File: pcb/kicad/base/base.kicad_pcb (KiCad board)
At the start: 2 copper layers, 348 parts, among them P1 J-Link SWD, P10 CONN_01X02, P11 CONN_01X02, P2 SMA, P3 CONN_01X02, P4 USB Micro B, P5 Button, P6 Button, P7 Button, P8 Button, P9 Button, Q1 IRLML2502, U1 SAMB11G18A-edit, U2 XBee-PRO_900HP, Y1 32.768kHz, Y2 26MHz

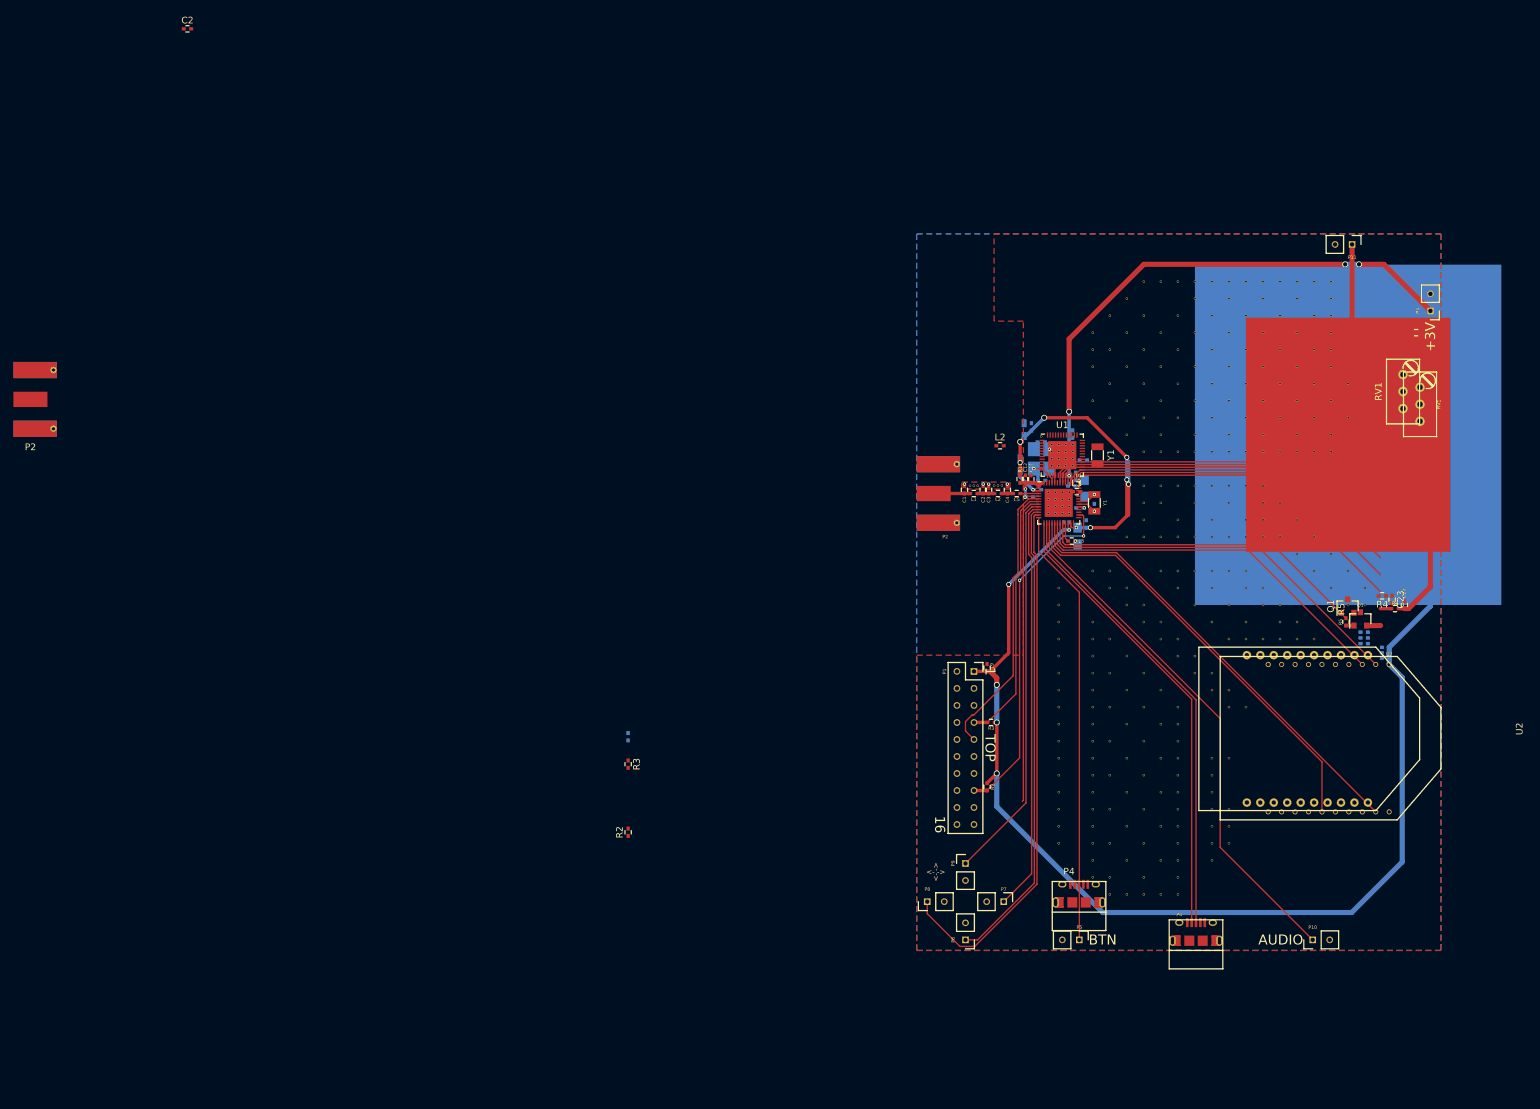
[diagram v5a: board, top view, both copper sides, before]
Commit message: Add stitch vias and fix silkscreen identifiers
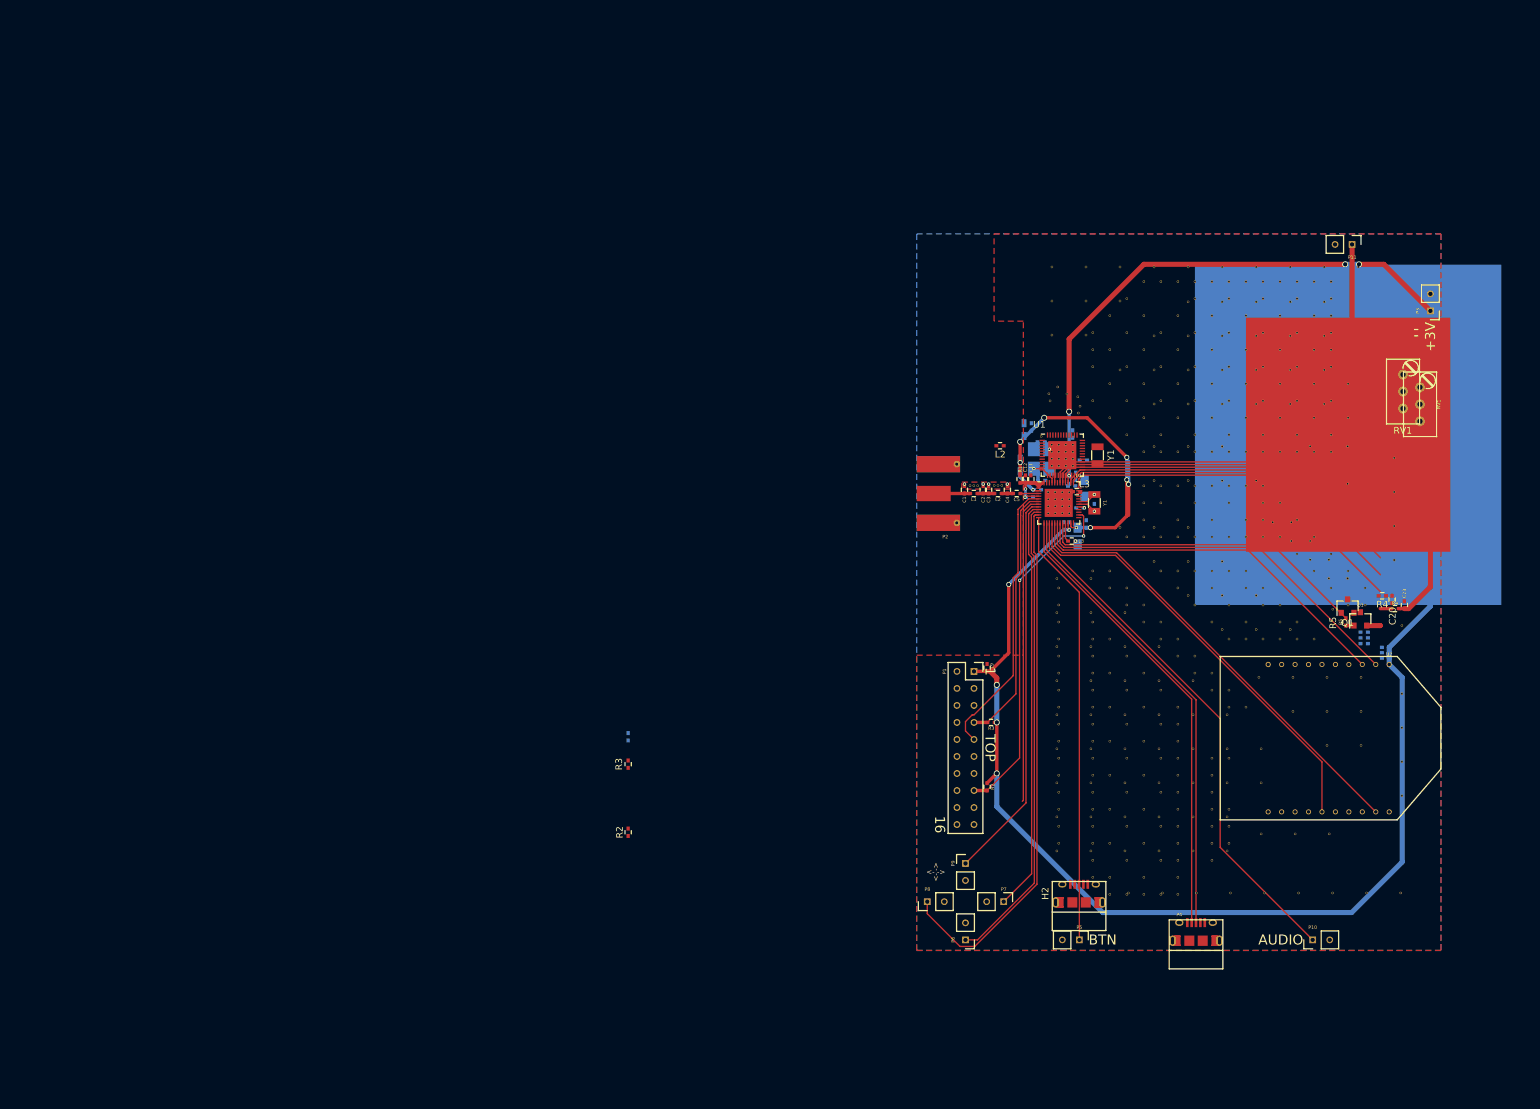
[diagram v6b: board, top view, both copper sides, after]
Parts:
- removed the C2 at (0.00, 0.00)
- removed the P2 at (-21.7, 55.3)
- removed the P4 at (133.1, 130.4)
- removed the U2 at (173.8, 104.5)
- added H2: USB Micro B, Connectors:USB_Micro-B_10118194-000XLF, F.Cu at (133.1, 130.4)
- added REF**: Via_Stitch_Dia0.356mm_Drill0.254mm, Misc:Via_Stitch_Dia0.356mm_Drill0.254mm, F.Cu at (181.1, 129.0)
- added REF**: Via_Stitch_Dia0.356mm_Drill0.254mm, Misc:Via_Stitch_Dia0.356mm_Drill0.254mm, F.Cu at (181.2, 114.5)
- added REF**: Via_Stitch_Dia0.356mm_Drill0.254mm, Misc:Via_Stitch_Dia0.356mm_Drill0.254mm, F.Cu at (144.2, 79.5)
- added REF**: Via_Stitch_Dia0.356mm_Drill0.254mm, Misc:Via_Stitch_Dia0.356mm_Drill0.254mm, F.Cu at (144.2, 74.4)
- added REF**: Via_Stitch_Dia0.356mm_Drill0.254mm, Misc:Via_Stitch_Dia0.356mm_Drill0.254mm, F.Cu at (149.3, 74.4)
- added REF**: Via_Stitch_Dia0.356mm_Drill0.254mm, Misc:Via_Stitch_Dia0.356mm_Drill0.254mm, F.Cu at (149.3, 79.5)
- added REF**: Via_Stitch_Dia0.356mm_Drill0.254mm, Misc:Via_Stitch_Dia0.356mm_Drill0.254mm, F.Cu at (169.6, 40.7)
- added REF**: Via_Stitch_Dia0.356mm_Drill0.254mm, Misc:Via_Stitch_Dia0.356mm_Drill0.254mm, F.Cu at (169.6, 45.8)
- added REF**: Via_Stitch_Dia0.356mm_Drill0.254mm, Misc:Via_Stitch_Dia0.356mm_Drill0.254mm, F.Cu at (169.6, 56.0)
- added REF**: Via_Stitch_Dia0.356mm_Drill0.254mm, Misc:Via_Stitch_Dia0.356mm_Drill0.254mm, F.Cu at (169.6, 50.9)
- added REF**: Via_Stitch_Dia0.356mm_Drill0.254mm, Misc:Via_Stitch_Dia0.356mm_Drill0.254mm, F.Cu at (164.6, 50.9)
- added REF**: Via_Stitch_Dia0.356mm_Drill0.254mm, Misc:Via_Stitch_Dia0.356mm_Drill0.254mm, F.Cu at (164.6, 56.0)
- added REF**: Via_Stitch_Dia0.356mm_Drill0.254mm, Misc:Via_Stitch_Dia0.356mm_Drill0.254mm, F.Cu at (181.2, 89.1)
- added REF**: Via_Stitch_Dia0.356mm_Drill0.254mm, Misc:Via_Stitch_Dia0.356mm_Drill0.254mm, F.Cu at (159.5, 56.0)
- added REF**: Via_Stitch_Dia0.356mm_Drill0.254mm, Misc:Via_Stitch_Dia0.356mm_Drill0.254mm, F.Cu at (159.5, 50.9)
- added REF**: Via_Stitch_Dia0.356mm_Drill0.254mm, Misc:Via_Stitch_Dia0.356mm_Drill0.254mm, F.Cu at (159.5, 40.7)
- added REF**: Via_Stitch_Dia0.356mm_Drill0.254mm, Misc:Via_Stitch_Dia0.356mm_Drill0.254mm, F.Cu at (159.5, 45.8)
- added REF**: Via_Stitch_Dia0.356mm_Drill0.254mm, Misc:Via_Stitch_Dia0.356mm_Drill0.254mm, F.Cu at (164.6, 45.8)
- added REF**: Via_Stitch_Dia0.356mm_Drill0.254mm, Misc:Via_Stitch_Dia0.356mm_Drill0.254mm, F.Cu at (164.6, 40.7)
- added REF**: Via_Stitch_Dia0.356mm_Drill0.254mm, Misc:Via_Stitch_Dia0.356mm_Drill0.254mm, F.Cu at (139.2, 50.9)
- added REF**: Via_Stitch_Dia0.356mm_Drill0.254mm, Misc:Via_Stitch_Dia0.356mm_Drill0.254mm, F.Cu at (154.4, 40.7)
- added REF**: Via_Stitch_Dia0.356mm_Drill0.254mm, Misc:Via_Stitch_Dia0.356mm_Drill0.254mm, F.Cu at (154.4, 45.8)
- added REF**: Via_Stitch_Dia0.356mm_Drill0.254mm, Misc:Via_Stitch_Dia0.356mm_Drill0.254mm, F.Cu at (149.3, 45.8)
- added REF**: Via_Stitch_Dia0.356mm_Drill0.254mm, Misc:Via_Stitch_Dia0.356mm_Drill0.254mm, F.Cu at (181.2, 109.4)
- added REF**: Via_Stitch_Dia0.356mm_Drill0.254mm, Misc:Via_Stitch_Dia0.356mm_Drill0.254mm, F.Cu at (149.3, 40.7)
- added REF**: Via_Stitch_Dia0.356mm_Drill0.254mm, Misc:Via_Stitch_Dia0.356mm_Drill0.254mm, F.Cu at (144.2, 45.8)
- added REF**: Via_Stitch_Dia0.356mm_Drill0.254mm, Misc:Via_Stitch_Dia0.356mm_Drill0.254mm, F.Cu at (144.2, 56.0)
- added REF**: Via_Stitch_Dia0.356mm_Drill0.254mm, Misc:Via_Stitch_Dia0.356mm_Drill0.254mm, F.Cu at (144.2, 50.9)
- added REF**: Via_Stitch_Dia0.356mm_Drill0.254mm, Misc:Via_Stitch_Dia0.356mm_Drill0.254mm, F.Cu at (149.3, 50.9)
- added REF**: Via_Stitch_Dia0.356mm_Drill0.254mm, Misc:Via_Stitch_Dia0.356mm_Drill0.254mm, F.Cu at (149.3, 56.0)
- added REF**: Via_Stitch_Dia0.356mm_Drill0.254mm, Misc:Via_Stitch_Dia0.356mm_Drill0.254mm, F.Cu at (154.4, 56.0)
- added REF**: Via_Stitch_Dia0.356mm_Drill0.254mm, Misc:Via_Stitch_Dia0.356mm_Drill0.254mm, F.Cu at (154.4, 50.9)
- added REF**: Via_Stitch_Dia0.356mm_Drill0.254mm, Misc:Via_Stitch_Dia0.356mm_Drill0.254mm, F.Cu at (159.5, 67.4)
- added REF**: Via_Stitch_Dia0.356mm_Drill0.254mm, Misc:Via_Stitch_Dia0.356mm_Drill0.254mm, F.Cu at (154.4, 62.3)
- added REF**: Via_Stitch_Dia0.356mm_Drill0.254mm, Misc:Via_Stitch_Dia0.356mm_Drill0.254mm, F.Cu at (181.2, 104.3)
- added REF**: Via_Stitch_Dia0.356mm_Drill0.254mm, Misc:Via_Stitch_Dia0.356mm_Drill0.254mm, F.Cu at (154.4, 67.4)
- added REF**: Via_Stitch_Dia0.356mm_Drill0.254mm, Misc:Via_Stitch_Dia0.356mm_Drill0.254mm, F.Cu at (149.3, 67.4)
- added REF**: Via_Stitch_Dia0.356mm_Drill0.254mm, Misc:Via_Stitch_Dia0.356mm_Drill0.254mm, F.Cu at (149.3, 62.3)
- added REF**: Via_Stitch_Dia0.356mm_Drill0.254mm, Misc:Via_Stitch_Dia0.356mm_Drill0.254mm, F.Cu at (144.2, 62.3)
- added REF**: Via_Stitch_Dia0.356mm_Drill0.254mm, Misc:Via_Stitch_Dia0.356mm_Drill0.254mm, F.Cu at (144.2, 67.4)
- added REF**: Via_Stitch_Dia0.356mm_Drill0.254mm, Misc:Via_Stitch_Dia0.356mm_Drill0.254mm, F.Cu at (173.1, 62.3)
- added REF**: Via_Stitch_Dia0.356mm_Drill0.254mm, Misc:Via_Stitch_Dia0.356mm_Drill0.254mm, F.Cu at (173.1, 67.9)
- added REF**: Via_Stitch_Dia0.356mm_Drill0.254mm, Misc:Via_Stitch_Dia0.356mm_Drill0.254mm, F.Cu at (167.5, 62.3)
- added REF**: Via_Stitch_Dia0.356mm_Drill0.254mm, Misc:Via_Stitch_Dia0.356mm_Drill0.254mm, F.Cu at (167.5, 76.4)
- added REF**: Via_Stitch_Dia0.356mm_Drill0.254mm, Misc:Via_Stitch_Dia0.356mm_Drill0.254mm, F.Cu at (164.7, 76.4)
- added REF**: Via_Stitch_Dia0.356mm_Drill0.254mm, Misc:Via_Stitch_Dia0.356mm_Drill0.254mm, F.Cu at (181.2, 99.2)
- added REF**: Via_Stitch_Dia0.356mm_Drill0.254mm, Misc:Via_Stitch_Dia0.356mm_Drill0.254mm, F.Cu at (162.0, 73.6)
- added REF**: Via_Stitch_Dia0.356mm_Drill0.254mm, Misc:Via_Stitch_Dia0.356mm_Drill0.254mm, F.Cu at (164.7, 73.6)
- added REF**: Via_Stitch_Dia0.356mm_Drill0.254mm, Misc:Via_Stitch_Dia0.356mm_Drill0.254mm, F.Cu at (170.3, 79.2)
- added REF**: Via_Stitch_Dia0.356mm_Drill0.254mm, Misc:Via_Stitch_Dia0.356mm_Drill0.254mm, F.Cu at (167.5, 79.2)
- added REF**: Via_Stitch_Dia0.356mm_Drill0.254mm, Misc:Via_Stitch_Dia0.356mm_Drill0.254mm, F.Cu at (170.3, 82.0)
- added REF**: Via_Stitch_Dia0.356mm_Drill0.254mm, Misc:Via_Stitch_Dia0.356mm_Drill0.254mm, F.Cu at (173.1, 82.0)
- added REF**: Via_Stitch_Dia0.356mm_Drill0.254mm, Misc:Via_Stitch_Dia0.356mm_Drill0.254mm, F.Cu at (132.9, 54.9)
- added REF**: Via_Stitch_Dia0.356mm_Drill0.254mm, Misc:Via_Stitch_Dia0.356mm_Drill0.254mm, F.Cu at (129.9, 53.4)
- added REF**: Via_Stitch_Dia0.356mm_Drill0.254mm, Misc:Via_Stitch_Dia0.356mm_Drill0.254mm, F.Cu at (128.5, 54.5)
- added REF**: Via_Stitch_Dia0.356mm_Drill0.254mm, Misc:Via_Stitch_Dia0.356mm_Drill0.254mm, F.Cu at (131.2, 54.5)
- added REF**: Via_Stitch_Dia0.356mm_Drill0.254mm, Misc:Via_Stitch_Dia0.356mm_Drill0.254mm, F.Cu at (129.7, 122.7)
- added REF**: Via_Stitch_Dia0.356mm_Drill0.254mm, Misc:Via_Stitch_Dia0.356mm_Drill0.254mm, F.Cu at (133.2, 56.3)
- added REF**: Via_Stitch_Dia0.356mm_Drill0.254mm, Misc:Via_Stitch_Dia0.356mm_Drill0.254mm, F.Cu at (132.9, 57.3)
- added REF**: Via_Stitch_Dia0.356mm_Drill0.254mm, Misc:Via_Stitch_Dia0.356mm_Drill0.254mm, F.Cu at (129.7, 117.6)
- added REF**: Via_Stitch_Dia0.356mm_Drill0.254mm, Misc:Via_Stitch_Dia0.356mm_Drill0.254mm, F.Cu at (129.7, 107.4)
- added REF**: Via_Stitch_Dia0.356mm_Drill0.254mm, Misc:Via_Stitch_Dia0.356mm_Drill0.254mm, F.Cu at (129.7, 112.5)
- added REF**: Via_Stitch_Dia0.356mm_Drill0.254mm, Misc:Via_Stitch_Dia0.356mm_Drill0.254mm, F.Cu at (129.7, 97.3)
- added REF**: Via_Stitch_Dia0.356mm_Drill0.254mm, Misc:Via_Stitch_Dia0.356mm_Drill0.254mm, F.Cu at (160.7, 129.0)
- added REF**: Via_Stitch_Dia0.356mm_Drill0.254mm, Misc:Via_Stitch_Dia0.356mm_Drill0.254mm, F.Cu at (129.7, 92.2)
- added REF**: Via_Stitch_Dia0.356mm_Drill0.254mm, Misc:Via_Stitch_Dia0.356mm_Drill0.254mm, F.Cu at (129.7, 102.4)
- added REF**: Via_Stitch_Dia0.356mm_Drill0.254mm, Misc:Via_Stitch_Dia0.356mm_Drill0.254mm, F.Cu at (129.7, 87.1)
- added REF**: Via_Stitch_Dia0.356mm_Drill0.254mm, Misc:Via_Stitch_Dia0.356mm_Drill0.254mm, F.Cu at (129.7, 82.0)
- added REF**: Via_Stitch_Dia0.356mm_Drill0.254mm, Misc:Via_Stitch_Dia0.356mm_Drill0.254mm, F.Cu at (180.1, 79.3)
- added REF**: Via_Stitch_Dia0.356mm_Drill0.254mm, Misc:Via_Stitch_Dia0.356mm_Drill0.254mm, F.Cu at (180.1, 74.2)
- added REF**: Via_Stitch_Dia0.356mm_Drill0.254mm, Misc:Via_Stitch_Dia0.356mm_Drill0.254mm, F.Cu at (180.1, 64.0)
- added REF**: Via_Stitch_Dia0.356mm_Drill0.254mm, Misc:Via_Stitch_Dia0.356mm_Drill0.254mm, F.Cu at (180.1, 69.1)
- added REF**: Via_Stitch_Dia0.356mm_Drill0.254mm, Misc:Via_Stitch_Dia0.356mm_Drill0.254mm, F.Cu at (129.0, 45.7)
- added REF**: Via_Stitch_Dia0.356mm_Drill0.254mm, Misc:Via_Stitch_Dia0.356mm_Drill0.254mm, F.Cu at (134.1, 45.7)
- added REF**: Via_Stitch_Dia0.356mm_Drill0.254mm, Misc:Via_Stitch_Dia0.356mm_Drill0.254mm, F.Cu at (165.8, 129.0)
- added REF**: Via_Stitch_Dia0.356mm_Drill0.254mm, Misc:Via_Stitch_Dia0.356mm_Drill0.254mm, F.Cu at (129.0, 35.5)
- added REF**: Via_Stitch_Dia0.356mm_Drill0.254mm, Misc:Via_Stitch_Dia0.356mm_Drill0.254mm, F.Cu at (134.1, 35.5)
- added REF**: Via_Stitch_Dia0.356mm_Drill0.254mm, Misc:Via_Stitch_Dia0.356mm_Drill0.254mm, F.Cu at (134.1, 40.6)
- added REF**: Via_Stitch_Dia0.356mm_Drill0.254mm, Misc:Via_Stitch_Dia0.356mm_Drill0.254mm, F.Cu at (129.0, 40.6)
- added REF**: Via_Stitch_Dia0.356mm_Drill0.254mm, Misc:Via_Stitch_Dia0.356mm_Drill0.254mm, F.Cu at (139.2, 40.6)
- added REF**: Via_Stitch_Dia0.356mm_Drill0.254mm, Misc:Via_Stitch_Dia0.356mm_Drill0.254mm, F.Cu at (154.4, 35.5)
- added REF**: Via_Stitch_Dia0.356mm_Drill0.254mm, Misc:Via_Stitch_Dia0.356mm_Drill0.254mm, F.Cu at (149.3, 35.5)
- added REF**: Via_Stitch_Dia0.356mm_Drill0.254mm, Misc:Via_Stitch_Dia0.356mm_Drill0.254mm, F.Cu at (139.2, 35.5)
- added REF**: Via_Stitch_Dia0.356mm_Drill0.254mm, Misc:Via_Stitch_Dia0.356mm_Drill0.254mm, F.Cu at (144.2, 35.5)
- added REF**: Via_Stitch_Dia0.356mm_Drill0.254mm, Misc:Via_Stitch_Dia0.356mm_Drill0.254mm, F.Cu at (164.6, 35.5)
- added REF**: Via_Stitch_Dia0.356mm_Drill0.254mm, Misc:Via_Stitch_Dia0.356mm_Drill0.254mm, F.Cu at (176.0, 129.0)
- added REF**: Via_Stitch_Dia0.356mm_Drill0.254mm, Misc:Via_Stitch_Dia0.356mm_Drill0.254mm, F.Cu at (159.5, 35.5)
- added REF**: Via_Stitch_Dia0.356mm_Drill0.254mm, Misc:Via_Stitch_Dia0.356mm_Drill0.254mm, F.Cu at (169.6, 35.5)
- added REF**: Via_Stitch_Dia0.356mm_Drill0.254mm, Misc:Via_Stitch_Dia0.356mm_Drill0.254mm, F.Cu at (174.7, 35.5)
- added REF**: Via_Stitch_Dia0.356mm_Drill0.254mm, Misc:Via_Stitch_Dia0.356mm_Drill0.254mm, F.Cu at (128.7, 55.5)
- added REF**: Via_Stitch_Dia0.356mm_Drill0.254mm, Misc:Via_Stitch_Dia0.356mm_Drill0.254mm, F.Cu at (170.1, 106.9)
- added REF**: Via_Stitch_Dia0.356mm_Drill0.254mm, Misc:Via_Stitch_Dia0.356mm_Drill0.254mm, F.Cu at (175.1, 106.9)
- added REF**: Via_Stitch_Dia0.356mm_Drill0.254mm, Misc:Via_Stitch_Dia0.356mm_Drill0.254mm, F.Cu at (175.1, 101.9)
- added REF**: Via_Stitch_Dia0.356mm_Drill0.254mm, Misc:Via_Stitch_Dia0.356mm_Drill0.254mm, F.Cu at (165.0, 101.9)
- added REF**: Via_Stitch_Dia0.356mm_Drill0.254mm, Misc:Via_Stitch_Dia0.356mm_Drill0.254mm, F.Cu at (170.1, 101.9)
- added REF**: Via_Stitch_Dia0.356mm_Drill0.254mm, Misc:Via_Stitch_Dia0.356mm_Drill0.254mm, F.Cu at (165.0, 96.8)
- added REF**: Via_Stitch_Dia0.356mm_Drill0.254mm, Misc:Via_Stitch_Dia0.356mm_Drill0.254mm, F.Cu at (159.9, 96.8)
- added REF**: Via_Stitch_Dia0.356mm_Drill0.254mm, Misc:Via_Stitch_Dia0.356mm_Drill0.254mm, F.Cu at (170.9, 129.0)
- added REF**: Via_Stitch_Dia0.356mm_Drill0.254mm, Misc:Via_Stitch_Dia0.356mm_Drill0.254mm, F.Cu at (170.1, 96.8)
- added REF**: Via_Stitch_Dia0.356mm_Drill0.254mm, Misc:Via_Stitch_Dia0.356mm_Drill0.254mm, F.Cu at (175.1, 96.8)
- added REF**: Via_Stitch_Dia0.356mm_Drill0.254mm, Misc:Via_Stitch_Dia0.356mm_Drill0.254mm, F.Cu at (170.4, 120.1)
- added REF**: Via_Stitch_Dia0.356mm_Drill0.254mm, Misc:Via_Stitch_Dia0.356mm_Drill0.254mm, F.Cu at (155.1, 117.6)
- added REF**: Via_Stitch_Dia0.356mm_Drill0.254mm, Misc:Via_Stitch_Dia0.356mm_Drill0.254mm, F.Cu at (155.1, 122.7)
- added REF**: Via_Stitch_Dia0.356mm_Drill0.254mm, Misc:Via_Stitch_Dia0.356mm_Drill0.254mm, F.Cu at (165.3, 120.1)
- added REF**: Via_Stitch_Dia0.356mm_Drill0.254mm, Misc:Via_Stitch_Dia0.356mm_Drill0.254mm, F.Cu at (160.2, 120.1)
- added REF**: Via_Stitch_Dia0.356mm_Drill0.254mm, Misc:Via_Stitch_Dia0.356mm_Drill0.254mm, F.Cu at (160.2, 112.5)
- added REF**: Via_Stitch_Dia0.356mm_Drill0.254mm, Misc:Via_Stitch_Dia0.356mm_Drill0.254mm, F.Cu at (160.2, 107.4)
- added REF**: Via_Stitch_Dia0.356mm_Drill0.254mm, Misc:Via_Stitch_Dia0.356mm_Drill0.254mm, F.Cu at (155.1, 107.4)
- added REF**: Via_Stitch_Dia0.356mm_Drill0.254mm, Misc:Via_Stitch_Dia0.356mm_Drill0.254mm, F.Cu at (150.6, 129.0)
- added REF**: Via_Stitch_Dia0.356mm_Drill0.254mm, Misc:Via_Stitch_Dia0.356mm_Drill0.254mm, F.Cu at (155.1, 112.5)
- added REF**: Via_Stitch_Dia0.356mm_Drill0.254mm, Misc:Via_Stitch_Dia0.356mm_Drill0.254mm, F.Cu at (155.1, 102.4)
- added REF**: Via_Stitch_Dia0.356mm_Drill0.254mm, Misc:Via_Stitch_Dia0.356mm_Drill0.254mm, F.Cu at (134.8, 82.0)
- added REF**: Via_Stitch_Dia0.356mm_Drill0.254mm, Misc:Via_Stitch_Dia0.356mm_Drill0.254mm, F.Cu at (134.8, 87.1)
- added REF**: Via_Stitch_Dia0.356mm_Drill0.254mm, Misc:Via_Stitch_Dia0.356mm_Drill0.254mm, F.Cu at (139.9, 87.1)
- added REF**: Via_Stitch_Dia0.356mm_Drill0.254mm, Misc:Via_Stitch_Dia0.356mm_Drill0.254mm, F.Cu at (134.8, 102.4)
- added REF**: Via_Stitch_Dia0.356mm_Drill0.254mm, Misc:Via_Stitch_Dia0.356mm_Drill0.254mm, F.Cu at (139.9, 102.4)
- added REF**: Via_Stitch_Dia0.356mm_Drill0.254mm, Misc:Via_Stitch_Dia0.356mm_Drill0.254mm, F.Cu at (139.9, 97.3)
- added REF**: Via_Stitch_Dia0.356mm_Drill0.254mm, Misc:Via_Stitch_Dia0.356mm_Drill0.254mm, F.Cu at (139.9, 92.2)
- added REF**: Via_Stitch_Dia0.356mm_Drill0.254mm, Misc:Via_Stitch_Dia0.356mm_Drill0.254mm, F.Cu at (134.8, 92.2)
- added REF**: Via_Stitch_Dia0.356mm_Drill0.254mm, Misc:Via_Stitch_Dia0.356mm_Drill0.254mm, F.Cu at (155.7, 129.0)
- added REF**: Via_Stitch_Dia0.356mm_Drill0.254mm, Misc:Via_Stitch_Dia0.356mm_Drill0.254mm, F.Cu at (134.8, 97.3)
- added REF**: Via_Stitch_Dia0.356mm_Drill0.254mm, Misc:Via_Stitch_Dia0.356mm_Drill0.254mm, F.Cu at (145.0, 97.3)
- added REF**: Via_Stitch_Dia0.356mm_Drill0.254mm, Misc:Via_Stitch_Dia0.356mm_Drill0.254mm, F.Cu at (145.0, 92.2)
- added REF**: Via_Stitch_Dia0.356mm_Drill0.254mm, Misc:Via_Stitch_Dia0.356mm_Drill0.254mm, F.Cu at (150.1, 97.3)
- added REF**: Via_Stitch_Dia0.356mm_Drill0.254mm, Misc:Via_Stitch_Dia0.356mm_Drill0.254mm, F.Cu at (150.1, 102.4)
- added REF**: Via_Stitch_Dia0.356mm_Drill0.254mm, Misc:Via_Stitch_Dia0.356mm_Drill0.254mm, F.Cu at (145.0, 102.4)
- added REF**: Via_Stitch_Dia0.356mm_Drill0.254mm, Misc:Via_Stitch_Dia0.356mm_Drill0.254mm, F.Cu at (145.0, 122.7)
- added REF**: Via_Stitch_Dia0.356mm_Drill0.254mm, Misc:Via_Stitch_Dia0.356mm_Drill0.254mm, F.Cu at (145.0, 117.6)
- added REF**: Via_Stitch_Dia0.356mm_Drill0.254mm, Misc:Via_Stitch_Dia0.356mm_Drill0.254mm, F.Cu at (150.1, 117.6)
- added REF**: Via_Stitch_Dia0.356mm_Drill0.254mm, Misc:Via_Stitch_Dia0.356mm_Drill0.254mm, F.Cu at (150.1, 122.7)
- added REF**: Via_Stitch_Dia0.356mm_Drill0.254mm, Misc:Via_Stitch_Dia0.356mm_Drill0.254mm, F.Cu at (145.5, 129.0)
- added REF**: Via_Stitch_Dia0.356mm_Drill0.254mm, Misc:Via_Stitch_Dia0.356mm_Drill0.254mm, F.Cu at (150.1, 112.5)
- added REF**: Via_Stitch_Dia0.356mm_Drill0.254mm, Misc:Via_Stitch_Dia0.356mm_Drill0.254mm, F.Cu at (150.1, 107.4)
- added REF**: Via_Stitch_Dia0.356mm_Drill0.254mm, Misc:Via_Stitch_Dia0.356mm_Drill0.254mm, F.Cu at (145.0, 107.4)
- added REF**: Via_Stitch_Dia0.356mm_Drill0.254mm, Misc:Via_Stitch_Dia0.356mm_Drill0.254mm, F.Cu at (145.0, 112.5)
- added REF**: Via_Stitch_Dia0.356mm_Drill0.254mm, Misc:Via_Stitch_Dia0.356mm_Drill0.254mm, F.Cu at (134.8, 112.5)
- added REF**: Via_Stitch_Dia0.356mm_Drill0.254mm, Misc:Via_Stitch_Dia0.356mm_Drill0.254mm, F.Cu at (134.8, 107.4)
- added REF**: Via_Stitch_Dia0.356mm_Drill0.254mm, Misc:Via_Stitch_Dia0.356mm_Drill0.254mm, F.Cu at (139.9, 107.4)
- added REF**: Via_Stitch_Dia0.356mm_Drill0.254mm, Misc:Via_Stitch_Dia0.356mm_Drill0.254mm, F.Cu at (139.9, 112.5)
- added REF**: Via_Stitch_Dia0.356mm_Drill0.254mm, Misc:Via_Stitch_Dia0.356mm_Drill0.254mm, F.Cu at (139.9, 122.7)
- added REF**: Via_Stitch_Dia0.356mm_Drill0.254mm, Misc:Via_Stitch_Dia0.356mm_Drill0.254mm, F.Cu at (139.9, 117.6)
- added REF**: Via_Stitch_Dia0.356mm_Drill0.254mm, Misc:Via_Stitch_Dia0.356mm_Drill0.254mm, F.Cu at (140.4, 129.0)
- added REF**: Via_Stitch_Dia0.356mm_Drill0.254mm, Misc:Via_Stitch_Dia0.356mm_Drill0.254mm, F.Cu at (134.8, 117.6)
- added REF**: Via_Stitch_Dia0.356mm_Drill0.254mm, Misc:Via_Stitch_Dia0.356mm_Drill0.254mm, F.Cu at (134.8, 122.7)
- added REF**: Via_Stitch_Dia0.356mm_Drill0.254mm, Misc:Via_Stitch_Dia0.356mm_Drill0.254mm, F.Cu at (164.6, 89.6)
- added REF**: Via_Stitch_Dia0.356mm_Drill0.254mm, Misc:Via_Stitch_Dia0.356mm_Drill0.254mm, F.Cu at (154.4, 79.5)
- added REF**: Via_Stitch_Dia0.356mm_Drill0.254mm, Misc:Via_Stitch_Dia0.356mm_Drill0.254mm, F.Cu at (149.3, 84.6)
- added REF**: Via_Stitch_Dia0.356mm_Drill0.254mm, Misc:Via_Stitch_Dia0.356mm_Drill0.254mm, F.Cu at (159.5, 89.6)
- added REF**: Via_Stitch_Dia0.356mm_Drill0.254mm, Misc:Via_Stitch_Dia0.356mm_Drill0.254mm, F.Cu at (159.5, 84.6)
- added REF**: Via_Stitch_Dia0.356mm_Drill0.254mm, Misc:Via_Stitch_Dia0.356mm_Drill0.254mm, F.Cu at (154.4, 84.6)
- added REF**: Via_Stitch_Dia0.356mm_Drill0.254mm, Misc:Via_Stitch_Dia0.356mm_Drill0.254mm, F.Cu at (154.4, 89.6)
- added REF**: Via_Stitch_Dia0.356mm_Drill0.254mm, Misc:Via_Stitch_Dia0.356mm_Drill0.254mm, F.Cu at (139.2, 74.4)
- C19: value C_Small -> 1.0uF
- C20: value 47pF -> 1.0uF; moved to F.Cu
- C21: value 1.0uF -> 47pF
- C22: value 10uF -> 1.0uF
- C23: value 1.0uF -> 10uF; moved to B.Cu
- moved C20 7.78 mm to (179.8, 85.2), turned to 270 degrees
- moved C23 6.41 mm to (175.6, 90.0), turned to 180 degrees
- moved C21 0.85 mm to (175.6, 91.7)
- moved C22 0.85 mm to (175.6, 90.9)
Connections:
- C20 pad 1: /+3.3V -> /+5V
- C23 pad 1: /+5V -> /+3.3V
- L2 pad 1: Net-(C2-Pad1) -> /SIG_2.4G
- REF** pad 1: (no net) -> /SIG_2.4G
- U1 pad 42: (no net) -> GND
- U1 pad 43: (no net) -> GND
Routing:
- net /SWDIO: track 0.00 -> 291.8 mm, vias 0 -> 9
- net /+3.3V: track 291.8 -> 0.99 mm, vias 9 -> 1
- net Net-(L3-Pad1): track 65.5 -> 0.00 mm
- net Net-(L3-Pad2): track 2.86 -> 65.5 mm
- net Net-(C18-Pad1): track 0.99 -> 43.9 mm, vias 1 -> 7
- net /+5V: track 0.00 -> 42.0 mm
- net Net-(C14-Pad1): track 43.9 -> 4.55 mm, vias 7 -> 1
- net /SWDCLK: track 38.9 -> 0.00 mm
- net Net-(C13-Pad1): track 4.55 -> 10.3 mm, vias 1 -> 2
- net Net-(C8-Pad1): track 7.20 -> 2.75 mm
- net Net-(C10-Pad1): track 10.3 -> 5.95 mm, vias 2 -> 1
- net /SWO: track 42.0 -> 38.9 mm
- net /UART_RTS: track 0.00 -> 2.86 mm
- net Net-(C2-Pad1): track 2.51 -> 0.00 mm
- net Net-(C9-Pad1): track 5.95 -> 7.20 mm
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
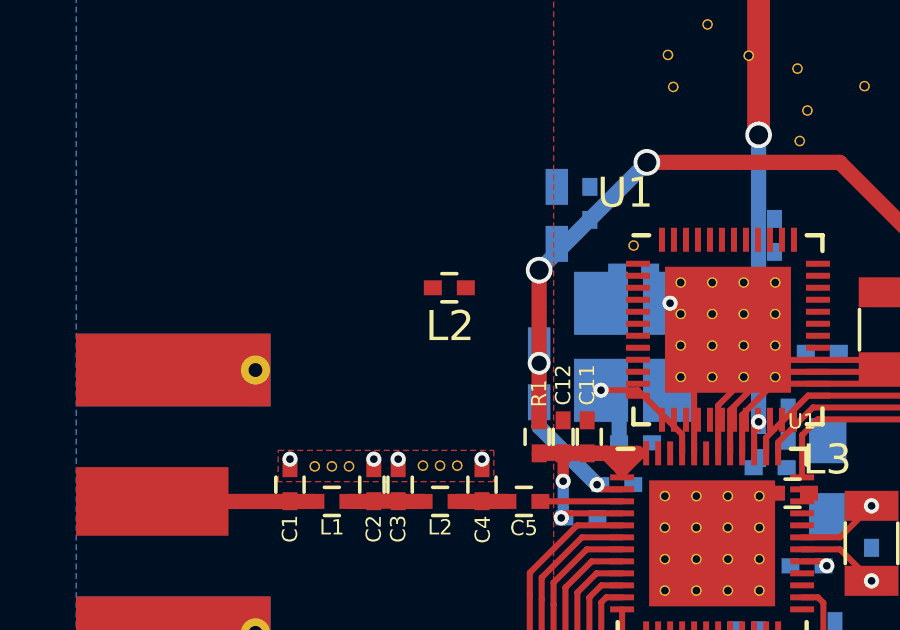
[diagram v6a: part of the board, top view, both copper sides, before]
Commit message: Add vertical SMA, matching stub, and dimensions
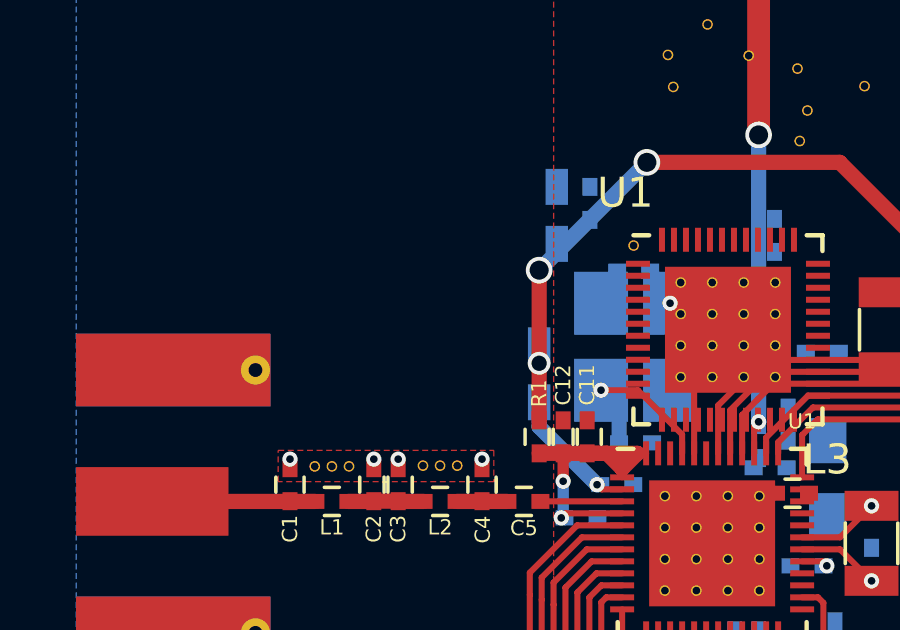
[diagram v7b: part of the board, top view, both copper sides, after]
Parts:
- removed the L2 at (121.3, 62.2)
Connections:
- H2 pad 1: (no net) -> /+5V_USB
- H2 pad 4: (no net) -> Net-(H2-Pad4)
- U1 pad 24: (no net) -> Net-(U1-Pad24)
- U1 pad 25: (no net) -> Net-(U1-Pad25)
- U1 pad 27: (no net) -> Net-(U1-Pad27)
- U1 pad 28: (no net) -> Net-(U1-Pad28)
- U1 pad 3: Net-(C5-Pad1) -> /SIG_2.4G
- U1 pad 33: (no net) -> Net-(U1-Pad33)
- U1 pad 34: (no net) -> Net-(U1-Pad34)
- U1 pad 35: (no net) -> Net-(U1-Pad35)
- U1 pad 46: (no net) -> Net-(U1-Pad46)
- U1 pad 47: (no net) -> Net-(U1-Pad47)
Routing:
- net /SWO: track 38.9 -> 291.8 mm, vias 0 -> 9
- net /SWDIO: track 291.8 -> 43.9 mm, vias 9 -> 7
- net Net-(U2-Pad19): track 0.00 -> 78.5 mm
- net 70: track 78.5 -> 0.00 mm
- net Net-(U2-Pad5): track 0.00 -> 70.2 mm
- net 76: track 70.2 -> 0.00 mm
- net Net-(U2-Pad11): track 0.00 -> 68.9 mm
- net 67: track 68.9 -> 0.00 mm
- net Net-(U2-Pad13): track 0.00 -> 68.8 mm
- net 66: track 68.8 -> 0.00 mm
- net Net-(DS1-Pad7): track 0.00 -> 67.7 mm
- net 45: track 67.7 -> 0.00 mm
- net /UART_CTS: track 0.00 -> 65.5 mm
- net Net-(U2-Pad4): track 0.00 -> 65.5 mm
- net 75: track 65.5 -> 0.00 mm
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
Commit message: Fix footprints for connectors and crystal
Unnecessary SMDs in the matching circuit and 0 ohm link removed from the
schematic. Certain resistor and capacitor values updated to new offical
BOM components.
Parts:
- removed the R1 at (125.9, 59.4)
- added REF**: Via_Stitch_Dia0.356mm_Drill0.254mm, Misc:Via_Stitch_Dia0.356mm_Drill0.254mm, F.Cu at (127.0, 54.9)
- added REF**: Via_Stitch_Dia0.356mm_Drill0.254mm, Misc:Via_Stitch_Dia0.356mm_Drill0.254mm, F.Cu at (129.1, 54.6)
- added REF**: Via_Stitch_Dia0.356mm_Drill0.254mm, Misc:Via_Stitch_Dia0.356mm_Drill0.254mm, F.Cu at (127.9, 54.7)
- added REF**: Via_Stitch_Dia0.356mm_Drill0.254mm, Misc:Via_Stitch_Dia0.356mm_Drill0.254mm, F.Cu at (128.5, 56.5)
- added REF**: Via_Stitch_Dia0.356mm_Drill0.254mm, Misc:Via_Stitch_Dia0.356mm_Drill0.254mm, F.Cu at (129.6, 59.0)
- added REF**: Via_Stitch_Dia0.356mm_Drill0.254mm, Misc:Via_Stitch_Dia0.356mm_Drill0.254mm, F.Cu at (129.0, 57.3)
- R2: value 10k -> 1k
- REF**: value Via_Stitch_Dia0.356mm_Drill0.254mm -> (none)
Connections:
- C14 pad 1: Net-(C14-Pad1) -> Net-(C10-Pad1)
- FB1 pad 1: Net-(C14-Pad1) -> Net-(C10-Pad1)
- L4 pad 2: Net-(C14-Pad1) -> Net-(C10-Pad1)
- REF** pad 1: GND -> /+3.3V
- U1 pad 23: Net-(C14-Pad1) -> Net-(C10-Pad1)
- U1 pad 30: Net-(C6-Pad1) -> GND
- U1 pad 31: Net-(C7-Pad1) -> GND
- Y1 pad 1: Net-(C6-Pad1) -> GND
- Y1 pad 2: Net-(C7-Pad1) -> GND
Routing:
- net /SWO: track 291.8 -> 4.55 mm, vias 9 -> 1
- net Net-(L3-Pad2): track 42.0 -> 291.8 mm, vias 0 -> 9
- net Net-(U2-Pad7): track 0.00 -> 78.5 mm
- net Net-(U2-Pad5): track 70.2 -> 0.00 mm
- net 76: track 0.00 -> 70.2 mm
- net Net-(U2-Pad11): track 68.9 -> 0.00 mm
- net Net-(U2-Pad13): track 68.8 -> 0.00 mm
- net Net-(DS1-Pad7): track 67.7 -> 0.00 mm
- net Net-(H1-Pad5): track 1.66 -> 67.7 mm
- net Net-(DS1-Pad15): track 0.00 -> 65.5 mm
- net Net-(U2-Pad4): track 65.5 -> 0.00 mm
- net 75: track 0.00 -> 65.5 mm
- net Net-(DS1-Pad8): track 64.6 -> 0.00 mm
- net Net-(H1-Pad2): track 56.1 -> 0.00 mm
- net Net-(U1-Pad33): track 0.00 -> 51.4 mm, vias 0 -> 2
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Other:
- board text added: "May 25, 2017"
- board text removed: "May 5, 2017"
